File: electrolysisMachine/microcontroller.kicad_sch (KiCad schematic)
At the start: 23 parts

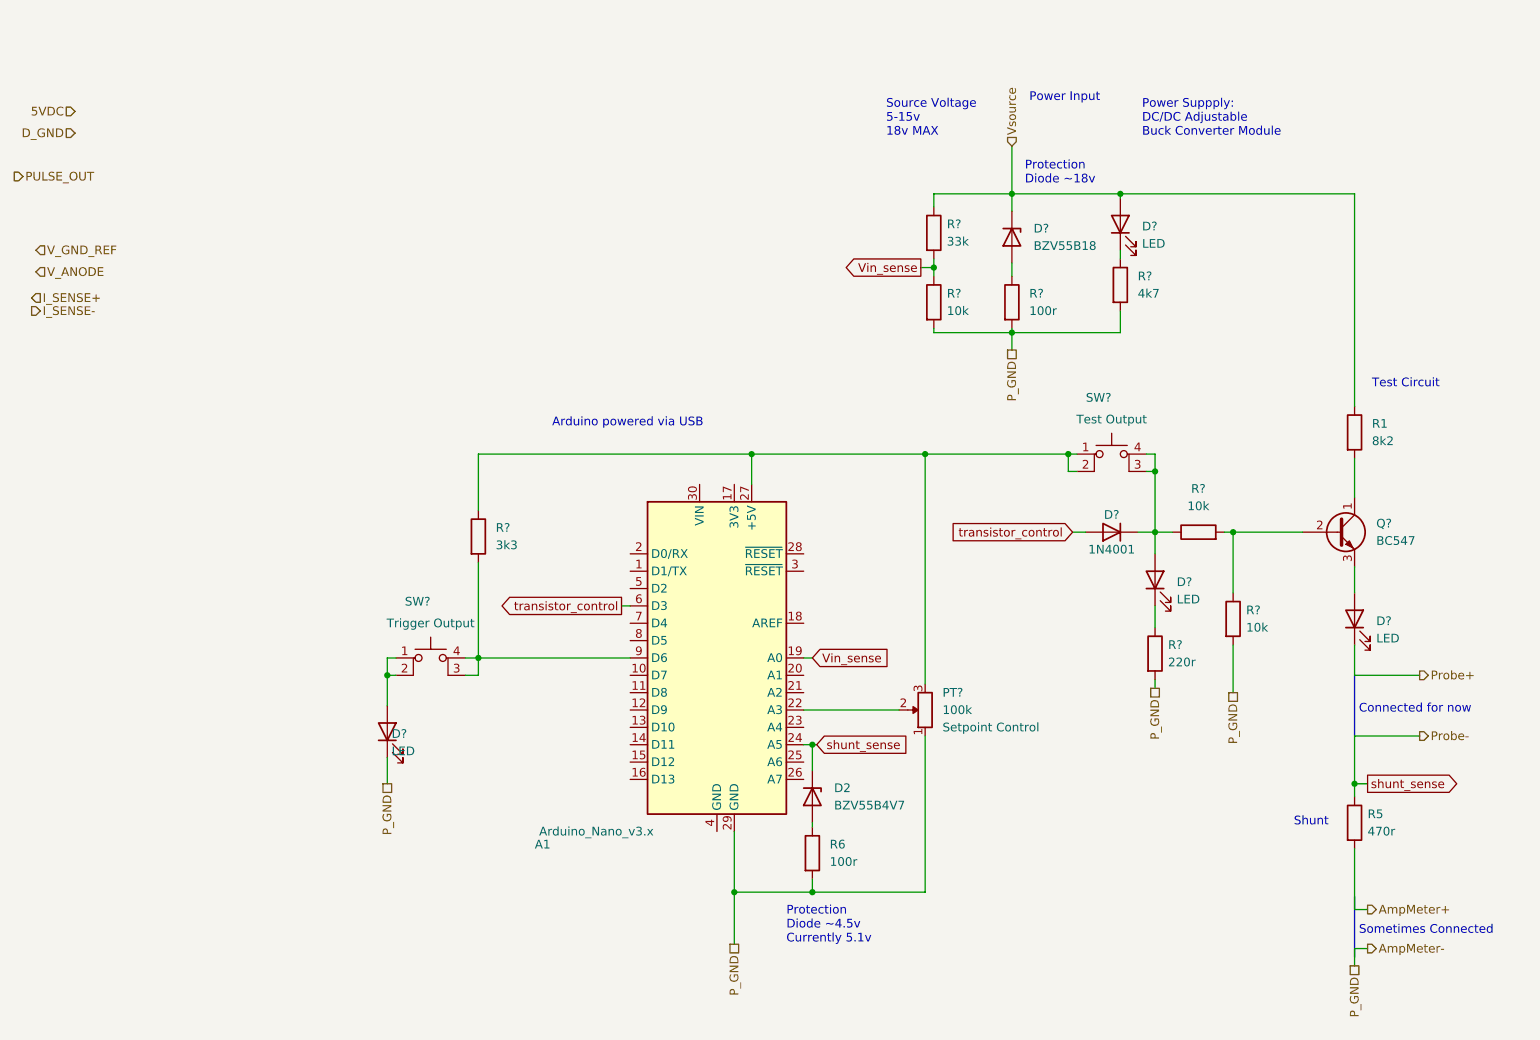
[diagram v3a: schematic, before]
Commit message: updated kicad schematic
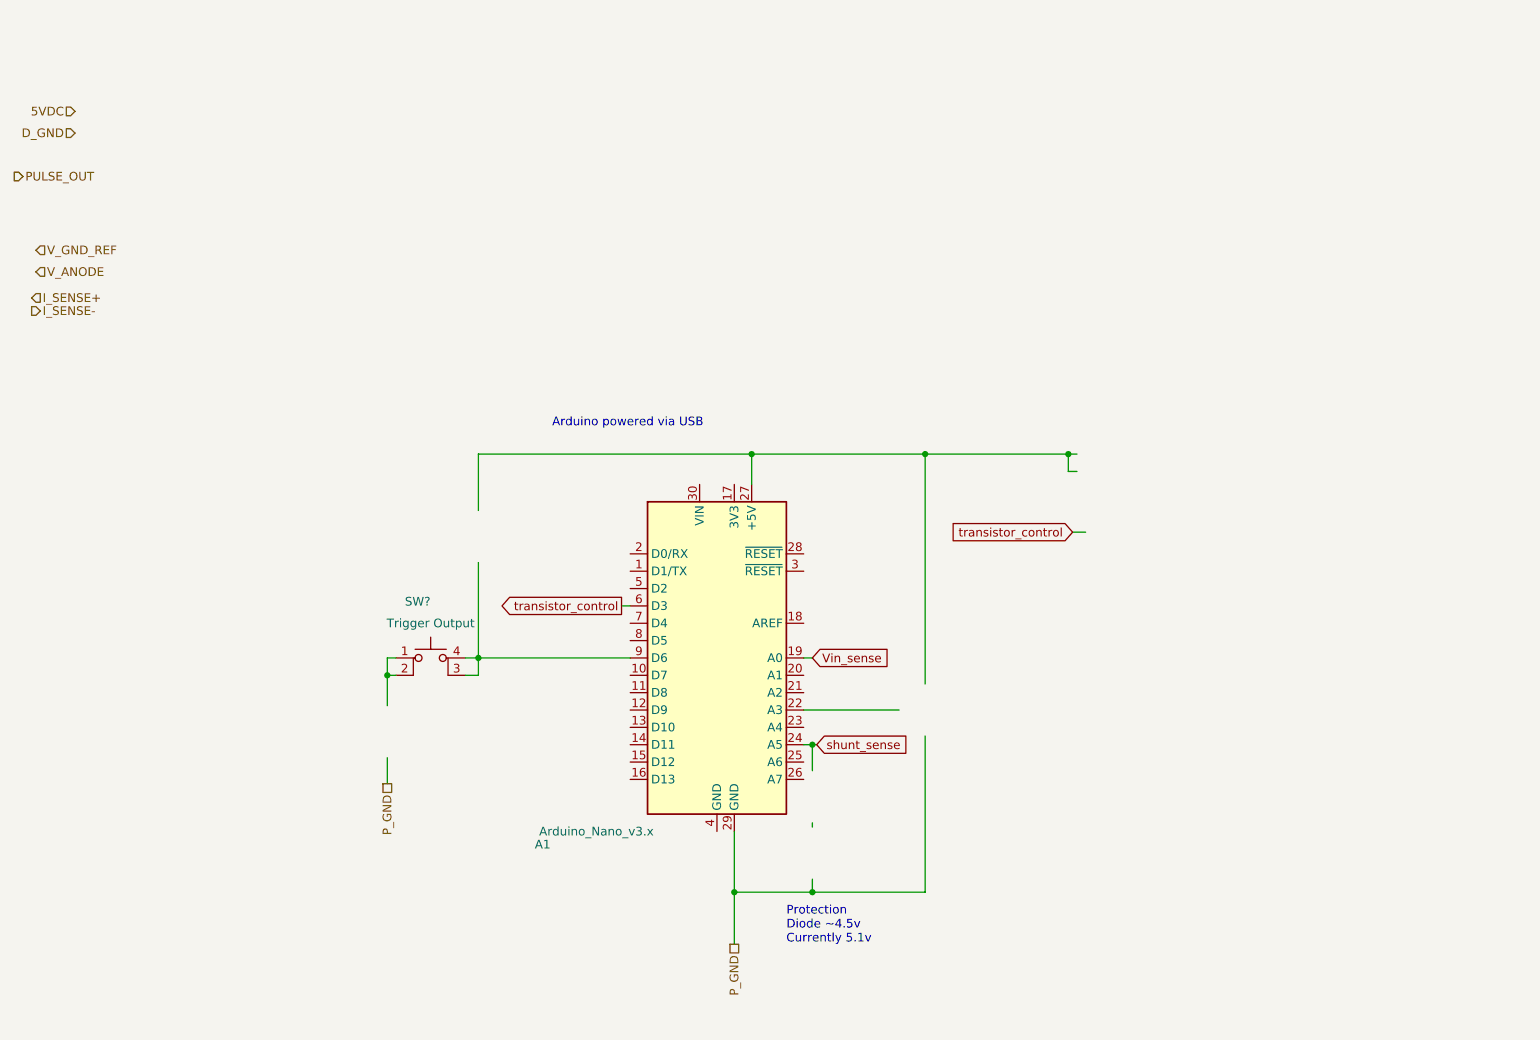
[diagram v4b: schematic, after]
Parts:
- removed D2: BZV55B4V7, Diode_SMD:D_MiniMELF, symbol Diode:BZV55B4V7
- removed D?: BZV55B18, Diode_SMD:D_MiniMELF, symbol Diode:BZV55B18
- removed D? (x4): LED, LED_SMD:LED_0805_2012Metric_Pad1.15x1.40mm_HandSolder, symbol Device:LED
- removed D?: 1N4001, Diode_THT:D_DO-41_SOD81_P10.16mm_Horizontal, symbol Diode:1N4001
- removed PT?: 100k, Potentiometer_THT:Potentiometer_Alpha_RD901F-40-00D_Single_Vertical_CircularHoles, symbol 000_Resistors_Immo:Potentiometer
- removed Q?: BC547, Package_TO_SOT_THT:TO-92_Inline, symbol Transistor_BJT:BC547
- removed R1: 8k2, Resistor_SMD:R_0805_2012Metric_Pad1.20x1.40mm_HandSolder, symbol 000_Resistors_Immo:Resistor_0805
- removed R5: 470r, Resistor_SMD:R_0805_2012Metric_Pad1.20x1.40mm_HandSolder, symbol 000_Resistors_Immo:Resistor_0805
- removed R6, R?: 100r, Resistor_SMD:R_0805_2012Metric_Pad1.20x1.40mm_HandSolder, symbol 000_Resistors_Immo:Resistor_0805
- removed R?: 3k3, Resistor_SMD:R_0805_2012Metric_Pad1.20x1.40mm_HandSolder, symbol 000_Resistors_Immo:Resistor_0805
- removed R?: 4k7, Resistor_SMD:R_0805_2012Metric_Pad1.20x1.40mm_HandSolder, symbol 000_Resistors_Immo:Resistor_0805
- removed R? (x3): 10k, Resistor_SMD:R_0805_2012Metric_Pad1.20x1.40mm_HandSolder, symbol 000_Resistors_Immo:Resistor_0805
- removed R?: 220r, Resistor_SMD:R_0805_2012Metric_Pad1.20x1.40mm_HandSolder, symbol 000_Resistors_Immo:Resistor_0805
- removed R?: 33k, Resistor_SMD:R_0805_2012Metric_Pad1.20x1.40mm_HandSolder, symbol 000_Resistors_Immo:Resistor_0805
- removed SW?: Test Output, symbol 000_Switches_Immo:pushbutton_tactile_4pin_th
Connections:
- net AmpMeter- renamed P_GND
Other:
- note removed: "Connected for now"
- note removed: "Power Input"
- note removed: "Power Suppply: DC/DC Adjustable Buck Converter Module"
- note removed: "Protection Diode ~18v"
- note removed: "Shunt"
- note removed: "Sometimes Connected"
- note removed: "Source Voltage 5-15v 18v MAX"
- note removed: "Test Circuit"
